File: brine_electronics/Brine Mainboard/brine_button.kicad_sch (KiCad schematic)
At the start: 1 part

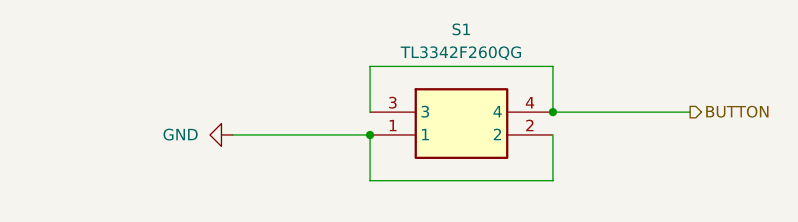
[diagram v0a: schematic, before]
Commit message: Resolved schematic DRC issues ✅
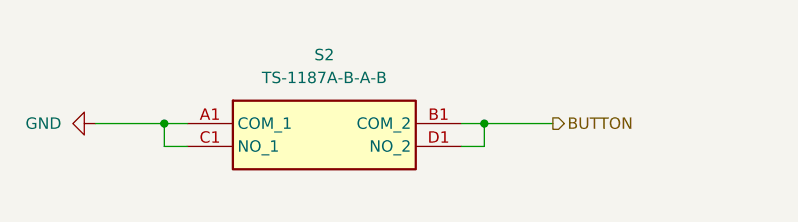
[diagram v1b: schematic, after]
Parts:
- removed S1: TL3342F260QG, TL3342F160QG:SW_TL3342F160QG, symbol 5_2mm_Button:TL3342F260QG
- added S2: TS-1187A-B-A-B, TS-1187A:TS1187ABAB, symbol TS-1187A-B-A-B:TS-1187A-B-A-B
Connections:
- net BUTTON: now also S2.B1 (COM_2), S2.D1 (NO_2)
- net GND: now also S2.A1 (COM_1), S2.C1 (NO_1)
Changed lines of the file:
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@@
 	(title_block
 		(title "Brine - Button")
-		(date "2026-04-03")
+		(date "2026-04-07")
 		(rev "1.0.0")
 		(company "Splendid Endeavors")
@@
 	)
 	(junction
-		(at 152.4 111.76)
+		(at 109.22 113.03)
 		(diameter 0)
 		(color 0 0 0 0)
 	)
 	(junction
-		(at 132.08 114.3)
+		(at 144.78 113.03)
 		(diameter 0)
 		(color 0 0 0 0)
@@
 	(wire
 		(pts
-			(xy 132.08 111.76) (xy 132.08 106.68)
-		)
-		(stroke
-			(width 0)
-			(type default)
-		)
-	)
-	(wire
-		(pts
-			(xy 152.4 119.38) (xy 152.4 114.3)
-		)
-		(stroke
-			(width 0)
-			(type default)
-		)
-	)
-	(wire
-		(pts
-			(xy 152.4 106.68) (xy 152.4 111.76)
-		)
-		(stroke
-			(width 0)
-			(type default)
-		)
-	)
-	(wire
-		(pts
-			(xy 132.08 119.38) (xy 152.4 119.38)
-		)
-		(stroke
-			(width 0)
-			(type default)
-		)
-	)
-	(wire
-		(pts
-			(xy 152.4 111.76) (xy 167.64 111.76)
-		)
-		(stroke
-			(width 0)
-			(type default)
-		)
-	)
-	(wire
-		(pts
-			(xy 116.84 114.3) (xy 132.08 114.3)
-		)
-		(stroke
-			(width 0)
-			(type default)
-		)
-	)
-	(wire
-		(pts
-			(xy 132.08 106.68) (xy 152.4 106.68)
-		)
-		(stroke
-			(width 0)
-			(type default)
-		)
-	)
-	(wire
-		(pts
-			(xy 132.08 114.3) (xy 132.08 119.38)
+			(xy 109.22 113.03) (xy 109.22 115.57)
+		)
+		(stroke
+			(width 0)
+			(type default)
+		)
+	)
+	(wire
+		(pts
+			(xy 101.6 113.03) (xy 109.22 113.03)
+		)
+		(stroke
+			(width 0)
+			(type default)
+		)
+	)
+	(wire
+		(pts
+			(xy 144.78 113.03) (xy 144.78 115.57)
+		)
+		(stroke
+			(width 0)
+			(type default)
+		)
+	)
+	(wire
+		(pts
+			(xy 142.24 113.03) (xy 144.78 113.03)
+		)
+		(stroke
+			(width 0)
+			(type default)
+		)
+	)
+	(wire
+		(pts
+			(xy 144.78 113.03) (xy 152.4 113.03)
+		)
+		(stroke
+			(width 0)
+			(type default)
+		)
+	)
+	(wire
+		(pts
+			(xy 142.24 115.57) (xy 144.78 115.57)
+		)
+		(stroke
+			(width 0)
+			(type default)
+		)
+	)
+	(wire
+		(pts
+			(xy 109.22 113.03) (xy 111.76 113.03)
+		)
+		(stroke
+			(width 0)
+			(type default)
+		)
+	)
+	(wire
+		(pts
+			(xy 111.76 115.57) (xy 109.22 115.57)
 		)
 		(stroke
@@
 	(hierarchical_label "BUTTON"
 		(shape output)
-		(at 167.64 111.76 0)
+		(at 152.4 113.03 0)
 		(effects
 			(font
@@
 	)
 	(symbol
-		(lib_id "5_2mm_Button:TL3342F260QG")
-		(at 132.08 111.76 0)
+		(lib_id "TS-1187A-B-A-B:TS-1187A-B-A-B")
+		(at 111.76 113.03 0)
 		(unit 1)
 		(exclude_from_sim no)
@@
 		(on_board yes)
 		(dnp no)
-		(property "Reference" "S1"
-			(at 142.24 102.616 0)
-			(effects
-				(font
-					(size 1.27 1.27)
-				)
-			)
-		)
-		(property "Value" "TL3342F260QG"
-			(at 142.24 105.156 0)
-			(effects
-				(font
-					(size 1.27 1.27)
-				)
-			)
-		)
-		(property "Footprint" "TL3342F160QG:SW_TL3342F160QG"
-			(at 148.59 206.68 0)
-			(effects
-				(font
-					(size 1.27 1.27)
-				)
-				(justify left top)
-				(hide yes)
-			)
-		)
-		(property "Datasheet" "https://configured-product-images.s3.amazonaws.com/2D/specs/TL3342F260QG.pdf"
-			(at 148.59 306.68 0)
-			(effects
-				(font
-					(size 1.27 1.27)
-				)
-				(justify left top)
-				(hide yes)
-			)
-		)
-		(property "Description" "TACT, 50mA, 12VDC SPST-NO, Off-(On) Surface Mount"
-			(at 132.08 111.76 0)
-			(effects
-				(font
-					(size 1.27 1.27)
-				)
-				(hide yes)
-			)
-		)
-		(property "Height" "1.54"
-			(at 148.59 506.68 0)
-			(effects
-				(font
-					(size 1.27 1.27)
-				)
-				(justify left top)
-				(hide yes)
-			)
-		)
-		(property "Mouser Part Number" "612-TL3342F260QG"
-			(at 148.59 606.68 0)
-			(effects
-				(font
-					(size 1.27 1.27)
-				)
-				(justify left top)
-				(hide yes)
-			)
-		)
-		(property "Mouser Price/Stock" "https://www.mouser.co.uk/ProductDetail/E-Switch/TL3342F260QG?qs=6C6BR4UgC3Of90YOH%2FEXyw%3D%3D"
-			(at 148.59 706.68 0)
-			(effects
-				(font
-					(size 1.27 1.27)
-				)
-				(justify left top)
-				(hide yes)
-			)
-		)
-		(property "Manufacturer_Name" "E-Switch"
-			(at 148.59 806.68 0)
-			(effects
-				(font
-					(size 1.27 1.27)
-				)
-				(justify left top)
-				(hide yes)
-			)
-		)
-		(property "Manufacturer_Part_Number" "TL3342F260QG"
-			(at 148.59 906.68 0)
-			(effects
-				(font
-					(size 1.27 1.27)
-				)
-				(justify left top)
-				(hide yes)
-			)
-		)
-		(pin "1"
-		)
-		(pin "3"
-		)
-		(pin "2"
-		)
-		(pin "4"
+		(fields_autoplaced yes)
+		(property "Reference" "S2"
+			(at 127 105.41 0)
+			(effects
+				(font
+					(size 1.27 1.27)
+				)
+			)
+		)
+		(property "Value" "TS-1187A-B-A-B"
+			(at 127 107.95 0)
+			(effects
+				(font
+					(size 1.27 1.27)
+				)
+			)
+		)
+		(property "Footprint" "TS-1187A:TS1187ABAB"
+			(at 138.43 207.95 0)
+			(effects
+				(font
+					(size 1.27 1.27)
+				)
+				(justify left top)
+				(hide yes)
+			)
+		)
+		(property "Datasheet" "http://www.helloxkb.com/public/images/pdf/TS-1187A-X-X-X.pdf"
+			(at 138.43 307.95 0)
+			(effects
+				(font
+					(size 1.27 1.27)
+				)
+				(justify left top)
+				(hide yes)
+			)
+		)
+		(property "Description" "tact switch 4x4X1.5 patch 160GF metal head waterproof"
+			(at 111.76 113.03 0)
+			(effects
+				(font
+					(size 1.27 1.27)
+				)
+				(hide yes)
+			)
+		)
+		(property "Height" "4.05"
+			(at 138.43 507.95 0)
+			(effects
+				(font
+					(size 1.27 1.27)
+				)
+				(justify left top)
+				(hide yes)
+			)
+		)
+		(property "Manufacturer_Name" "XKB Connectivity"
+			(at 138.43 607.95 0)
+			(effects
+				(font
+					(size 1.27 1.27)
+				)
+				(justify left top)
+				(hide yes)
+			)
+		)
+		(property "Manufacturer_Part_Number" "TS-1187A-B-A-B"
+			(at 138.43 707.95 0)
+			(effects
+				(font
+					(size 1.27 1.27)
+				)
+				(justify left top)
+				(hide yes)
+			)
+		)
+		(property "Mouser Part Number" ""
+			(at 138.43 807.95 0)
+			(effects
+				(font
+					(size 1.27 1.27)
+				)
+				(justify left top)
+				(hide yes)
+			)
+		)
+		(property "Mouser Price/Stock" ""
+			(at 138.43 907.95 0)
+			(effects
+				(font
+					(size 1.27 1.27)
+				)
+				(justify left top)
+				(hide yes)
+			)
+		)
+		(property "Arrow Part Number" ""
+			(at 138.43 1007.95 0)
+			(effects
+				(font
+					(size 1.27 1.27)
+				)
+				(justify left top)
+				(hide yes)
+			)
+		)
+		(property "Arrow Price/Stock" ""
+			(at 138.43 1107.95 0)
+			(effects
+				(font
+					(size 1.27 1.27)
+				)
+				(justify left top)
+				(hide yes)
+			)
+		)
+		(pin "C1"
+		)
+		(pin "D1"
+		)
+		(pin "A1"
+		)
+		(pin "B1"
 		)
 		(instances
-			(project "Brine"
+			(project ""
 				(path "/da3a4ef2-0e38-46f1-a1fc-55d8e0a83a54/4ad0d7d6-d3bf-4825-b971-cd4fdc149c91"
-					(reference "S1")
+					(reference "S2")
 					(unit 1)
 				)
@@
 	(symbol
 		(lib_id "power:GND")
-		(at 116.84 114.3 270)
+		(at 101.6 113.03 270)
 		(unit 1)
 		(exclude_from_sim no)
@@
 		(fields_autoplaced yes)
 		(property "Reference" "#PWR09"
-			(at 110.49 114.3 0)
+			(at 95.25 113.03 0)
 			(effects
 				(font
@@
 		)
 		(property "Value" "GND"
-			(at 113.03 114.2999 90)
+			(at 97.79 113.0299 90)
 			(effects
 				(font
@@
 		)
 		(property "Footprint" ""
-			(at 116.84 114.3 0)
+			(at 101.6 113.03 0)
 			(effects
 				(font
@@
 		)
 		(property "Datasheet" ""
-			(at 116.84 114.3 0)
+			(at 101.6 113.03 0)
 			(effects
 				(font
@@
 		)
 		(property "Description" "Power symbol creates a global label with name \"GND\" , ground"
-			(at 116.84 114.3 0)
-			(effects
-				(font
+			(at 101.6 113.03 0)
+			(effects
+				(font

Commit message: Updated button wiring :bug:
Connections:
- net BUTTON: now also S2.C1 (NO_1); no longer S2.B1 (COM_2)
- net GND: now also S2.B1 (COM_2); no longer S2.C1 (NO_1)
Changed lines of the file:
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@@
 	)
 	(junction
-		(at 109.22 113.03)
-		(diameter 0)
-		(color 0 0 0 0)
-	)
-	(junction
-		(at 144.78 113.03)
+		(at 152.4 115.57)
 		(diameter 0)
 		(color 0 0 0 0)
@@
 	(wire
 		(pts
-			(xy 109.22 113.03) (xy 109.22 115.57)
+			(xy 109.22 115.57) (xy 109.22 121.92)
 		)
 		(stroke
@@
 	(wire
 		(pts
-			(xy 101.6 113.03) (xy 109.22 113.03)
+			(xy 142.24 113.03) (xy 152.4 113.03)
 		)
 		(stroke
@@
 	(wire
 		(pts
-			(xy 144.78 113.03) (xy 144.78 115.57)
-		)
-		(stroke
-			(width 0)
-			(type default)
-		)
-	)
-	(wire
-		(pts
-			(xy 142.24 113.03) (xy 144.78 113.03)
-		)
-		(stroke
-			(width 0)
-			(type default)
-		)
-	)
-	(wire
-		(pts
-			(xy 144.78 113.03) (xy 152.4 113.03)
-		)
-		(stroke
-			(width 0)
-			(type default)
-		)
-	)
-	(wire
-		(pts
-			(xy 142.24 115.57) (xy 144.78 115.57)
-		)
-		(stroke
-			(width 0)
-			(type default)
-		)
-	)
-	(wire
-		(pts
-			(xy 109.22 113.03) (xy 111.76 113.03)
+			(xy 152.4 115.57) (xy 165.1 115.57)
 		)
 		(stroke
@@
 		)
 	)
+	(wire
+		(pts
+			(xy 152.4 115.57) (xy 152.4 121.92)
+		)
+		(stroke
+			(width 0)
+			(type default)
+		)
+	)
+	(wire
+		(pts
+			(xy 101.6 113.03) (xy 111.76 113.03)
+		)
+		(stroke
+			(width 0)
+			(type default)
+		)
+	)
+	(wire
+		(pts
+			(xy 142.24 115.57) (xy 152.4 115.57)
+		)
+		(stroke
+			(width 0)
+			(type default)
+		)
+	)
+	(wire
+		(pts
+			(xy 109.22 121.92) (xy 152.4 121.92)
+		)
+		(stroke
+			(width 0)
+			(type default)
+		)
+	)
 	(hierarchical_label "BUTTON"
 		(shape output)
-		(at 152.4 113.03 0)
+		(at 165.1 115.57 0)
 		(effects
 			(font
@@
 		)
 	)
+	(symbol
+		(lib_id "power:GND")
+		(at 152.4 113.03 90)
+		(unit 1)
+		(body_style 1)
+		(exclude_from_sim no)
+		(in_bom yes)
+		(on_board yes)
+		(in_pos_files yes)
+		(dnp no)
+		(fields_autoplaced yes)
+		(property "Reference" "#PWR030"
+			(at 158.75 113.03 0)
+			(hide yes)
+			(show_name no)
+			(do_not_autoplace no)
+			(effects
+				(font
+					(size 1.27 1.27)
+				)
+			)
+		)
+		(property "Value" "GND"
+			(at 156.21 113.0299 90)
+			(show_name no)
+			(do_not_autoplace no)
+			(effects
+				(font
+					(size 1.27 1.27)
+				)
+				(justify right)
+			)
+		)
+		(property "Footprint" ""
+			(at 152.4 113.03 0)
+			(hide yes)
+			(show_name no)
+			(do_not_autoplace no)
+			(effects
+				(font
+					(size 1.27 1.27)
+				)
+			)
+		)
+		(property "Datasheet" ""
+			(at 152.4 113.03 0)
+			(hide yes)
+			(show_name no)
+			(do_not_autoplace no)
+			(effects
+				(font
+					(size 1.27 1.27)
+				)
+			)
+		)
+		(property "Description" "Power symbol creates a global label with name \"GND\" , ground"
+			(at 152.4 113.03 0)
+			(hide yes)
+			(show_name no)
+			(do_not_autoplace no)
+			(effects
+				(font
+					(size 1.27 1.27)
+				)
+			)
+		)
+		(pin "1"
+		)
+		(instances
+			(project "Brine"
+				(path "/da3a4ef2-0e38-46f1-a1fc-55d8e0a83a54/4ad0d7d6-d3bf-4825-b971-cd4fdc149c91"
+					(reference "#PWR030")
+					(unit 1)
+				)
+			)
+		)
+	)

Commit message: Updated production files 🏭
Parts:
- S2: LCSC Part # (none) -> C318884; Manufacturer_Part_Number TS-1187A-B-A-B -> (none)
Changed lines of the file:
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@@
-			)
-		)
-		(property "Manufacturer_Part_Number" "TS-1187A-B-A-B"
-			(at 138.43 707.95 0)
-			(hide yes)
-			(show_name no)
-			(do_not_autoplace no)
-			(effects
-				(font
-					(size 1.27 1.27)
-				)
-				(justify left top)
 			)
 		)
@@
 			)
 		)
+		(property "Color" ""
+			(at 111.76 113.03 0)
+			(hide yes)
+			(show_name no)
+			(do_not_autoplace no)
+			(effects
+				(font
+					(size 1.27 1.27)
+				)
+			)
+		)
+		(property "LCSC Part #" "C318884"
+			(at 111.76 113.03 0)
+			(hide yes)
+			(show_name no)
+			(do_not_autoplace no)
+			(effects
+				(font
+					(size 1.27 1.27)
+				)
+			)
+		)

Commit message: Updated electronics production files 🏭
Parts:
- S2: JLCPCB Part # (none) -> C318884; LCSC Part # C318884 -> (none)
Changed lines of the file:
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@@
 			)
 		)
-		(property "LCSC Part #" "C318884"
+		(property "JLCPCB Part #" "C318884"
 			(at 111.76 113.03 0)
 			(hide yes)
